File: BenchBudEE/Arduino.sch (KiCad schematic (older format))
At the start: 23 parts

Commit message: Layout Work Session 16
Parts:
- removed R16: R, ~, symbol R
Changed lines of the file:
@@
 Sheet 7 9
 Title ""
-Date "16 mar 2014"
+Date "17 mar 2014"
 Rev ""
 Comp ""
@@
 	7700 5550 7700 5850
 $Comp
-L GND #PWR043
+L GND #PWR52
 U 1 1 52F7FF5C
 P 7700 5850
-F 0 "#PWR043" H 7700 5850 30  0001 C CNN
+F 0 "#PWR52" H 7700 5850 30  0001 C CNN
 F 1 "GND" H 7700 5780 30  0001 C CNN
 F 2 "" H 7700 5850 60  0000 C CNN
@@
 	2400 4650 2400 4450
 $Comp
-L +12P #PWR044
+L +12P #PWR50
 U 1 1 52FACD63
 P 2400 4450
-F 0 "#PWR044" H 2400 4420 30  0001 C CNN
+F 0 "#PWR50" H 2400 4420 30  0001 C CNN
 F 1 "+12P" H 2400 4550 30  0000 C CNN
 F 2 "" H 2400 4450 60  0000 C CNN
@@
 	1    0    0    -1
 $EndComp
-Wire Wire Line
-	2400 4200 2400 3950
-$Comp
-L +5V #PWR045
-U 1 1 5300B8CD
-P 2400 3950
-F 0 "#PWR045" H 2400 4040 20  0001 C CNN
-F 1 "+5V" H 2400 4040 30  0000 C CNN
-F 2 "" H 2400 3950 60  0000 C CNN
-F 3 "" H 2400 3950 60  0000 C CNN
-	1    2400 3950
-	1    0    0    -1
-$EndComp
-$Comp
-L R R16
-U 1 1 5300B8E0
-P 3300 4200
-F 0 "R16" V 3380 4200 40  0000 C CNN
-F 1 "R" V 3307 4201 40  0000 C CNN
-F 2 "~" V 3230 4200 30  0000 C CNN
-F 3 "~" H 3300 4200 30  0000 C CNN
-	1    3300 4200
-	0    1    1    0
-$EndComp
 $Comp
 L R R17
@@
 $EndComp
 Wire Wire Line
-	3550 4200 3700 4200
-Wire Wire Line
 	3700 4350 3550 4350
 Wire Wire Line
 	3700 4500 3550 4500
-Wire Wire Line
-	3050 4200 2400 4200
 Wire Wire Line
 	3050 4350 2800 4350
@@
 Connection ~ 2800 4500
 $Comp
-L GND #PWR046
+L GND #PWR51
 U 1 1 5300B9FD
 P 2800 4550
-F 0 "#PWR046" H 2800 4550 30  0001 C CNN
+F 0 "#PWR51" H 2800 4550 30  0001 C CNN
 F 1 "GND" H 2800 4480 30  0001 C CNN
 F 2 "" H 2800 4550 60  0000 C CNN

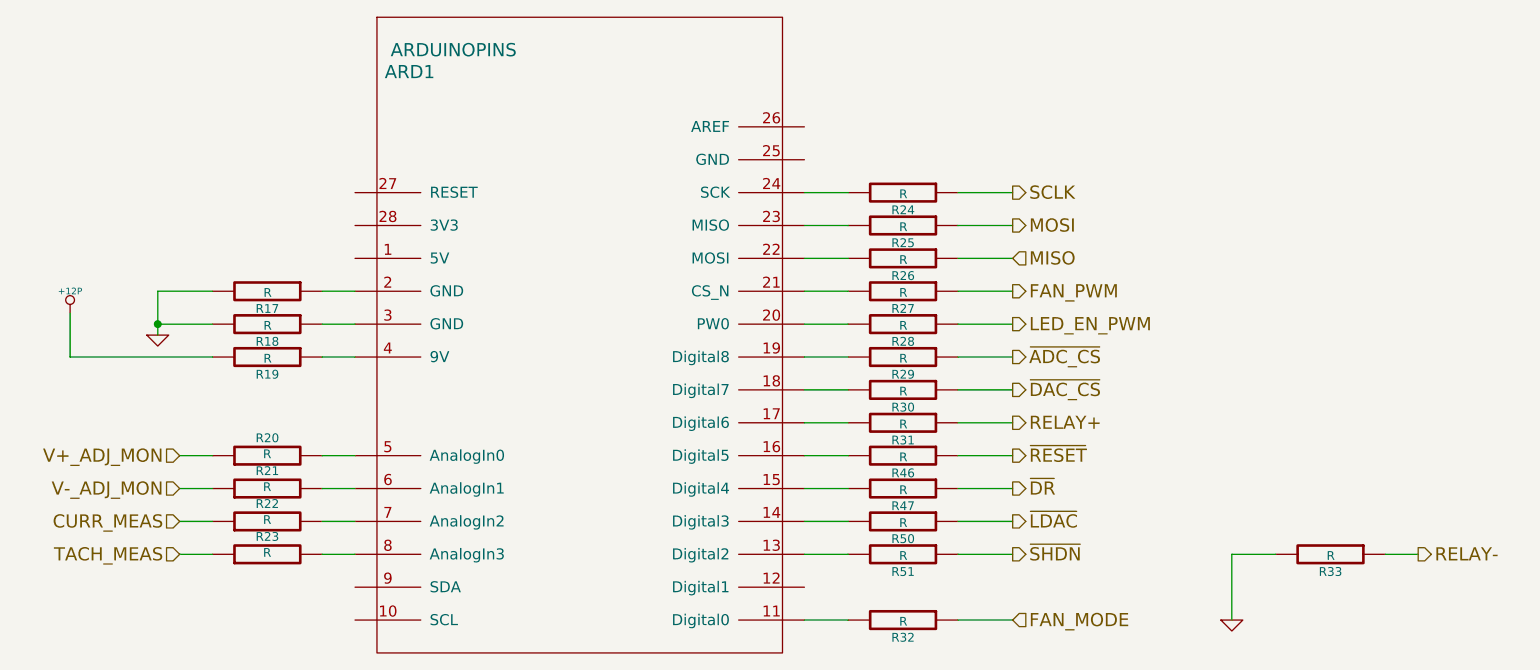
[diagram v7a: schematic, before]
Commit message: Changes for the BOM and BOMs
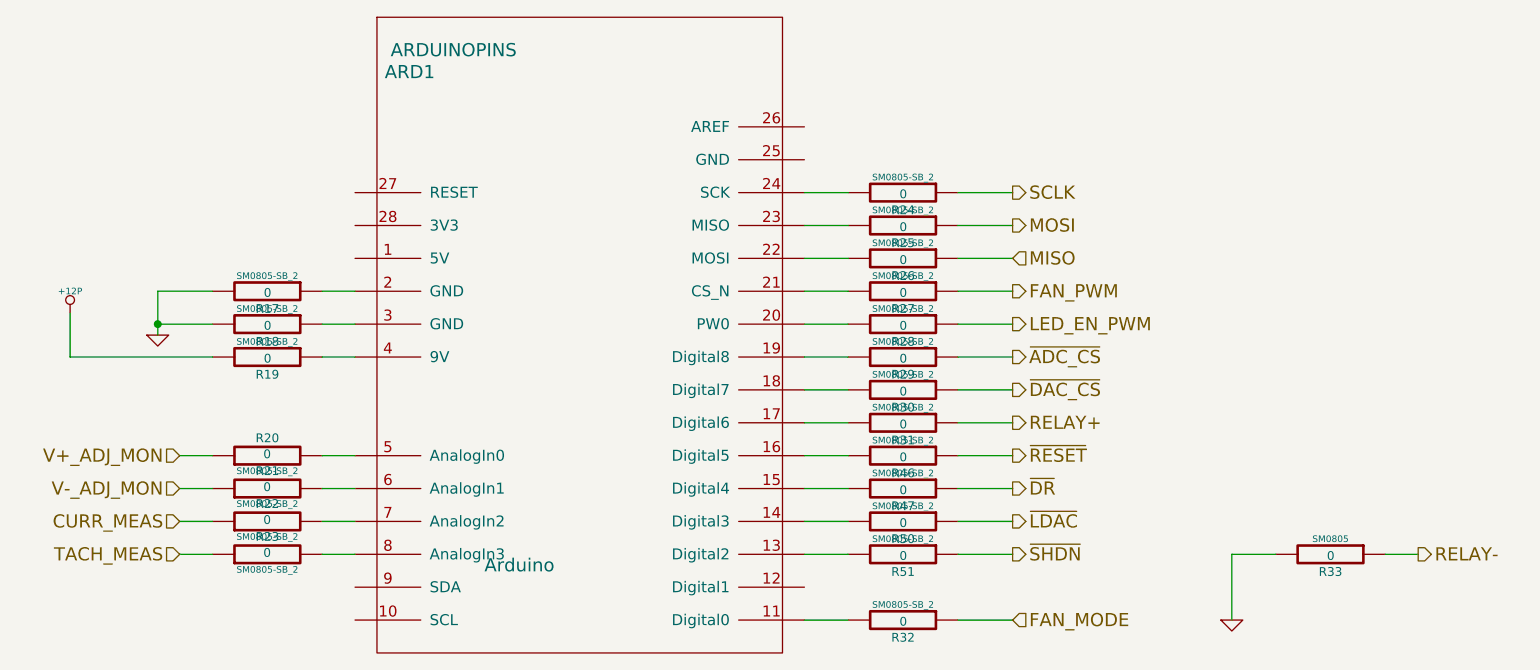
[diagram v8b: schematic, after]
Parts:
- ARD1: footprint ~ -> Arduino
- R17, R18, R19, R20, R21, R22, R23, R24, R25, R26, R27, R28, R29, R30, R31, R32, R46, R47, R50, R51: value R -> 0; footprint ~ -> SM0805-SB_2
- R33: value R -> 0; footprint ~ -> SM0805
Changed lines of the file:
@@
 Sheet 7 9
 Title ""
-Date "26 mar 2014"
+Date "26 apr 2014"
 Rev ""
 Comp ""
@@
 P 6200 4350
 F 0 "R27" V 6280 4350 40  0000 C CNN
-F 1 "R" V 6207 4351 40  0000 C CNN
-F 2 "~" V 6130 4350 30  0000 C CNN
+F 1 "0" V 6207 4351 40  0000 C CNN
+F 2 "SM0805-SB_2" V 6130 4350 30  0000 C CNN
 F 3 "~" H 6200 4350 30  0000 C CNN
 	1    6200 4350
@@
 P 6200 4950
 F 0 "R31" V 6280 4950 40  0000 C CNN
-F 1 "R" V 6207 4951 40  0000 C CNN
-F 2 "~" V 6130 4950 30  0000 C CNN
+F 1 "0" V 6207 4951 40  0000 C CNN
+F 2 "SM0805-SB_2" V 6130 4950 30  0000 C CNN
 F 3 "~" H 6200 4950 30  0000 C CNN
 	1    6200 4950
@@
 P 3300 5400
 F 0 "R22" V 3380 5400 40  0000 C CNN
-F 1 "R" V 3307 5401 40  0000 C CNN
-F 2 "~" V 3230 5400 30  0000 C CNN
+F 1 "0" V 3307 5401 40  0000 C CNN
+F 2 "SM0805-SB_2" V 3230 5400 30  0000 C CNN
 F 3 "~" H 3300 5400 30  0000 C CNN
 	1    3300 5400
@@
 P 3300 5550
 F 0 "R23" V 3380 5550 40  0000 C CNN
-F 1 "R" V 3307 5551 40  0000 C CNN
-F 2 "~" V 3230 5550 30  0000 C CNN
+F 1 "0" V 3307 5551 40  0000 C CNN
+F 2 "SM0805-SB_2" V 3230 5550 30  0000 C CNN
 F 3 "~" H 3300 5550 30  0000 C CNN
 	1    3300 5550
@@
 P 3300 5250
 F 0 "R21" V 3380 5250 40  0000 C CNN
-F 1 "R" V 3307 5251 40  0000 C CNN
-F 2 "~" V 3230 5250 30  0000 C CNN
+F 1 "0" V 3307 5251 40  0000 C CNN
+F 2 "SM0805-SB_2" V 3230 5250 30  0000 C CNN
 F 3 "~" H 3300 5250 30  0000 C CNN
 	1    3300 5250
@@
 P 3300 5100
 F 0 "R20" V 3380 5100 40  0000 C CNN
-F 1 "R" V 3307 5101 40  0000 C CNN
-F 2 "~" V 3230 5100 30  0000 C CNN
+F 1 "0" V 3307 5101 40  0000 C CNN
+F 2 "SM0805-SB_2" V 3230 5100 30  0000 C CNN
 F 3 "~" H 3300 5100 30  0000 C CNN
 	1    3300 5100
@@
 P 6200 4800
 F 0 "R30" V 6280 4800 40  0000 C CNN
-F 1 "R" V 6207 4801 40  0000 C CNN
-F 2 "~" V 6130 4800 30  0000 C CNN
+F 1 "0" V 6207 4801 40  0000 C CNN
+F 2 "SM0805-SB_2" V 6130 4800 30  0000 C CNN
 F 3 "~" H 6200 4800 30  0000 C CNN
 	1    6200 4800
@@
 P 6200 4200
 F 0 "R26" V 6280 4200 40  0000 C CNN
-F 1 "R" V 6207 4201 40  0000 C CNN
-F 2 "~" V 6130 4200 30  0000 C CNN
+F 1 "0" V 6207 4201 40  0000 C CNN
+F 2 "SM0805-SB_2" V 6130 4200 30  0000 C CNN
 F 3 "~" H 6200 4200 30  0000 C CNN
 	1    6200 4200
@@
 P 6200 4050
 F 0 "R25" V 6280 4050 40  0000 C CNN
-F 1 "R" V 6207 4051 40  0000 C CNN
-F 2 "~" V 6130 4050 30  0000 C CNN
+F 1 "0" V 6207 4051 40  0000 C CNN
+F 2 "SM0805-SB_2" V 6130 4050 30  0000 C CNN
 F 3 "~" H 6200 4050 30  0000 C CNN
 	1    6200 4050
@@
 P 6200 3900
 F 0 "R24" V 6280 3900 40  0000 C CNN
-F 1 "R" V 6207 3901 40  0000 C CNN
-F 2 "~" V 6130 3900 30  0000 C CNN
+F 1 "0" V 6207 3901 40  0000 C CNN
+F 2 "SM0805-SB_2" V 6130 3900 30  0000 C CNN
 F 3 "~" H 6200 3900 30  0000 C CNN
 	1    6200 3900
@@
 P 8150 5550
 F 0 "R33" V 8230 5550 40  0000 C CNN
-F 1 "R" V 8157 5551 40  0000 C CNN
-F 2 "~" V 8080 5550 30  0000 C CNN
+F 1 "0" V 8157 5551 40  0000 C CNN
+F 2 "SM0805" V 8080 5550 30  0000 C CNN
 F 3 "~" H 8150 5550 30  0000 C CNN
 	1    8150 5550
@@
 P 6200 4500
 F 0 "R28" V 6280 4500 40  0000 C CNN
-F 1 "R" V 6207 4501 40  0000 C CNN
-F 2 "~" V 6130 4500 30  0000 C CNN
+F 1 "0" V 6207 4501 40  0000 C CNN
+F 2 "SM0805-SB_2" V 6130 4500 30  0000 C CNN
 F 3 "~" H 6200 4500 30  0000 C CNN
 	1    6200 4500
@@
 P 6200 4650
 F 0 "R29" V 6280 4650 40  0000 C CNN
-F 1 "R" V 6207 4651 40  0000 C CNN
-F 2 "~" V 6130 4650 30  0000 C CNN
+F 1 "0" V 6207 4651 40  0000 C CNN
+F 2 "SM0805-SB_2" V 6130 4650 30  0000 C CNN
 F 3 "~" H 6200 4650 30  0000 C CNN
 	1    6200 4650
@@
 P 6200 5850
 F 0 "R32" V 6280 5850 40  0000 C CNN
-F 1 "R" V 6207 5851 40  0000 C CNN
-F 2 "~" V 6130 5850 30  0000 C CNN
+F 1 "0" V 6207 5851 40  0000 C CNN
+F 2 "SM0805-SB_2" V 6130 5850 30  0000 C CNN
 F 3 "~" H 6200 5850 30  0000 C CNN
 	1    6200 5850
@@
 P 3300 4650
 F 0 "R19" V 3380 4650 40  0000 C CNN
-F 1 "R" V 3307 4651 40  0000 C CNN
-F 2 "~" V 3230 4650 30  0000 C CNN
+F 1 "0" V 3307 4651 40  0000 C CNN
+F 2 "SM0805-SB_2" V 3230 4650 30  0000 C CNN
 F 3 "~" H 3300 4650 30  0000 C CNN
 	1    3300 4650
@@
 F 0 "ARD1" H 3950 5950 60  0000 C CNN
 F 1 "ARDUINOPINS" H 4150 6050 60  0000 C CNN
-F 2 "~" H 4450 3700 60  0000 C CNN
+F 2 "Arduino" H 4450 3700 60  0000 C CNN
 F 3 "~" H 4450 3700 60  0000 C CNN
 	1    4750 4650
@@
 P 3300 4350
 F 0 "R17" V 3380 4350 40  0000 C CNN
-F 1 "R" V 3307 4351 40  0000 C CNN
-F 2 "~" V 3230 4350 30  0000 C CNN
+F 1 "0" V 3307 4351 40  0000 C CNN
+F 2 "SM0805-SB_2" V 3230 4350 30  0000 C CNN
 F 3 "~" H 3300 4350 30  0000 C CNN
 	1    3300 4350
@@
 P 3300 4500
 F 0 "R18" V 3380 4500 40  0000 C CNN
-F 1 "R" V 3307 4501 40  0000 C CNN
-F 2 "~" V 3230 4500 30  0000 C CNN
+F 1 "0" V 3307 4501 40  0000 C CNN
+F 2 "SM0805-SB_2" V 3230 4500 30  0000 C CNN
 F 3 "~" H 3300 4500 30  0000 C CNN
 	1    3300 4500
@@
 P 6200 5250
 F 0 "R47" V 6280 5250 40  0000 C CNN
-F 1 "R" V 6207 5251 40  0000 C CNN
-F 2 "~" V 6130 5250 30  0000 C CNN
+F 1 "0" V 6207 5251 40  0000 C CNN
+F 2 "SM0805-SB_2" V 6130 5250 30  0000 C CNN
 F 3 "~" H 6200 5250 30  0000 C CNN
 	1    6200 5250
@@
 P 6200 5100
 F 0 "R46" V 6280 5100 40  0000 C CNN
-F 1 "R" V 6207 5101 40  0000 C CNN
-F 2 "~" V 6130 5100 30  0000 C CNN
+F 1 "0" V 6207 5101 40  0000 C CNN
+F 2 "SM0805-SB_2" V 6130 5100 30  0000 C CNN
 F 3 "~" H 6200 5100 30  0000 C CNN
 	1    6200 5100
@@
 P 6200 5400
 F 0 "R50" V 6280 5400 40  0000 C CNN
-F 1 "R" V 6207 5401 40  0000 C CNN
-F 2 "~" V 6130 5400 30  0000 C CNN
+F 1 "0" V 6207 5401 40  0000 C CNN
+F 2 "SM0805-SB_2" V 6130 5400 30  0000 C CNN
 F 3 "~" H 6200 5400 30  0000 C CNN
 	1    6200 5400
@@
 P 6200 5550
 F 0 "R51" V 6280 5550 40  0000 C CNN
-F 1 "R" V 6207 5551 40  0000 C CNN
-F 2 "~" V 6130 5550 30  0000 C CNN
+F 1 "0" V 6207 5551 40  0000 C CNN
+F 2 "SM0805-SB_2" V 6130 5550 30  0000 C CNN
 F 3 "~" H 6200 5550 30  0000 C CNN
 	1    6200 5550
